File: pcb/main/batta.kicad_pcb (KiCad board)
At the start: 2 copper layers, 126.9 x 99.3 mm, 42 parts

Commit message: clean router in batta main
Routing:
- net P6: track 157.1 -> 163.2 mm
- net P5: track 152.9 -> 158.8 mm
- net P4: track 172.2 -> 178.1 mm
- net P8: track 86.8 -> 90.3 mm
- net P1: track 142.3 -> 139.5 mm
- net P15: track 152.4 -> 149.6 mm
- net P18: track 138.9 -> 136.1 mm
- net P3: track 139.5 -> 141.9 mm
- net P14: track 89.2 -> 86.9 mm
- net P2: track 157.0 -> 155.3 mm
- net P0: track 183.1 -> 181.4 mm
- net GND: track 274.9 -> 275.8 mm

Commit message: updated gerber
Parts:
- removed the REF** at (103.8, -88.1)
- added REF**: Tenting Puck, kbd:Tenting_Puck2, F.Cu at (103.6, -88.1)

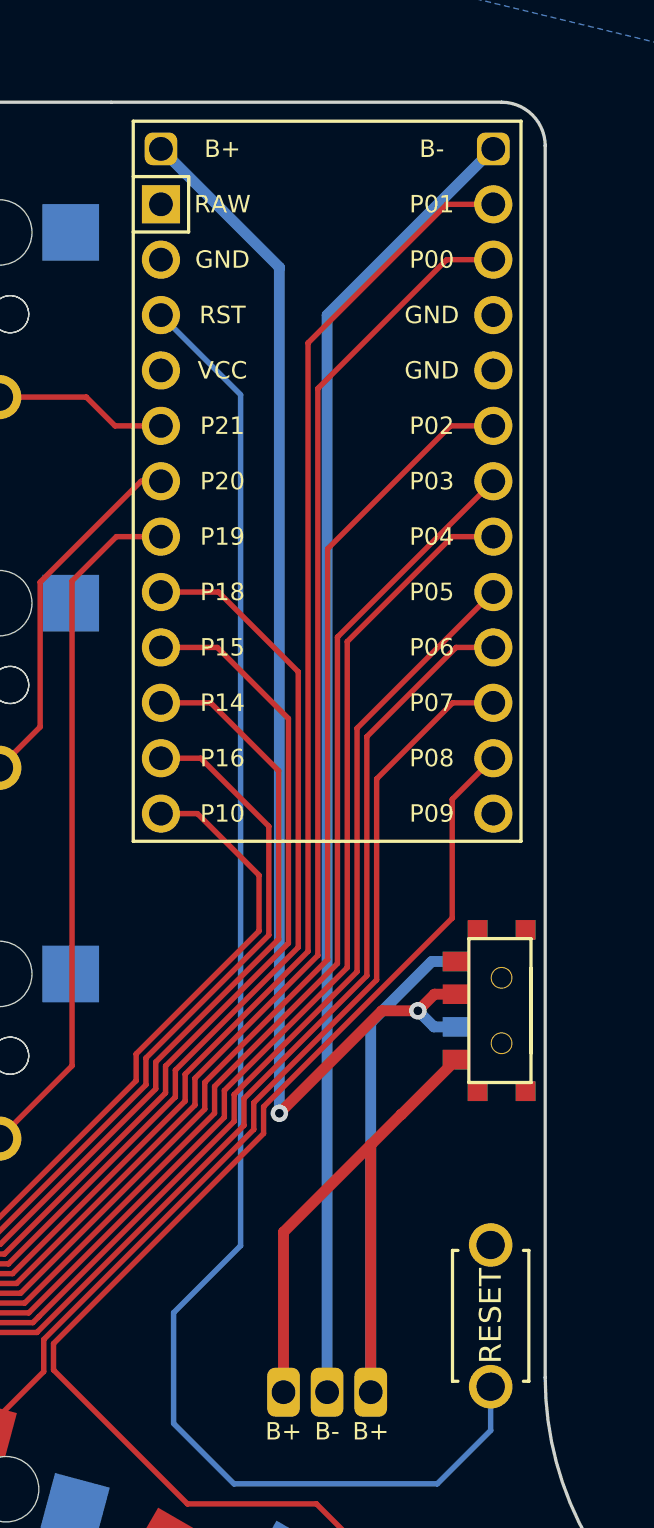
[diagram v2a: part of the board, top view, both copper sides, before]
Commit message: remove b- and b+
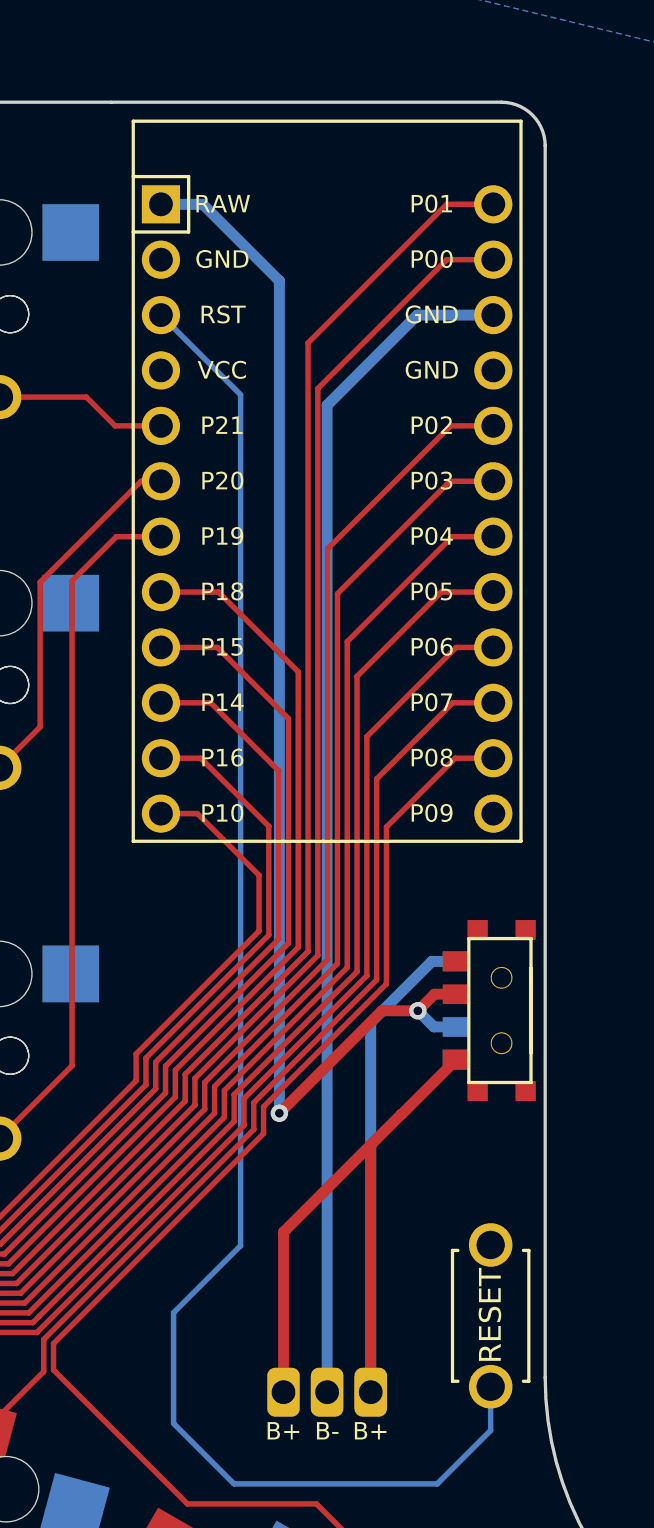
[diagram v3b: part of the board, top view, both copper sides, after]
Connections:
- MCU1 pad 15: GND -> Bminus
- T1 pad 2: Bplus -> RAW
- T2 pad 2: Bplus -> RAW
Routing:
- net Bplus: track 58.9 -> 0.00 mm, vias 2 -> 0
- net RAW: track 0.00 -> 57.5 mm, vias 0 -> 2
- net Bminus: track 60.2 -> 54.6 mm
- net P5: track 158.8 -> 160.2 mm
- net P3: track 141.9 -> 143.1 mm
- net P8: track 90.3 -> 91.3 mm
